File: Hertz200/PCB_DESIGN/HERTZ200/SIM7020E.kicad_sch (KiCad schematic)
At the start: 33 parts, among them J1 SMA_CONNECTOR, J2 SIM_Card, Q2 BC847, SW2 SW_Push, U2 SIM7020E, U3 TXB0104PW

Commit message: layout02
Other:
- moved on the sheet: D6
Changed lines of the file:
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@@
     (company "NANOHERTZ")
   )
-  (junction (at 41.91 127) (diameter 0) (color 0 0 0 0)
-  )
   (junction (at 78.74 163.83) (diameter 0) (color 0 0 0 0)
   )
@@
   (junction (at 199.39 113.03) (diameter 0) (color 0 0 0 0)
   )
+  (junction (at 86.36 124.46) (diameter 0) (color 0 0 0 0)
+  )
   (junction (at 41.91 110.49) (diameter 0) (color 0 0 0 0)
   )
-  (junction (at 31.75 110.49) (diameter 0) (color 0 0 0 0)
-  )
   (junction (at 52.07 124.46) (diameter 0) (color 0 0 0 0)
   )
@@
   )
   (junction (at 237.49 40.64) (diameter 0) (color 0 0 0 0)
+  )
+  (junction (at 97.79 110.49) (diameter 0) (color 0 0 0 0)
+  )
+  (junction (at 86.36 110.49) (diameter 0) (color 0 0 0 0)
   )
   (junction (at 74.93 124.46) (diameter 0) (color 0 0 0 0)
@@
     (stroke (width 0) (type default) (color 0 0 0 0))
   )
-  (wire (pts (xy 41.91 127) (xy 41.91 128.27))
+  (wire (pts (xy 41.91 124.46) (xy 41.91 128.27))
     (stroke (width 0) (type default) (color 0 0 0 0))
   )
@@
     (stroke (width 0) (type default) (color 0 0 0 0))
   )
+  (wire (pts (xy 86.36 127) (xy 86.36 124.46))
+    (stroke (width 0) (type default) (color 0 0 0 0))
+  )
+  (wire (pts (xy 97.79 127) (xy 86.36 127))
+    (stroke (width 0) (type default) (color 0 0 0 0))
+  )
   (wire (pts (xy 52.07 119.38) (xy 52.07 124.46))
     (stroke (width 0) (type default) (color 0 0 0 0))
@@
     (stroke (width 0) (type default) (color 0 0 0 0))
   )
-  (wire (pts (xy 31.75 127) (xy 41.91 127))
-    (stroke (width 0) (type default) (color 0 0 0 0))
-  )
   (wire (pts (xy 52.07 184.15) (xy 62.23 184.15))
     (stroke (width 0) (type default) (color 0 0 0 0))
   )
-  (wire (pts (xy 31.75 106.68) (xy 31.75 110.49))
-    (stroke (width 0) (type default) (color 0 0 0 0))
-  )
   (wire (pts (xy 139.7 162.56) (xy 140.97 162.56))
     (stroke (width 0) (type default) (color 0 0 0 0))
   )
+  (wire (pts (xy 86.36 110.49) (xy 97.79 110.49))
+    (stroke (width 0) (type default) (color 0 0 0 0))
+  )
   (wire (pts (xy 62.23 175.26) (xy 62.23 184.15))
     (stroke (width 0) (type default) (color 0 0 0 0))
@@
     (stroke (width 0) (type default) (color 0 0 0 0))
   )
-  (wire (pts (xy 31.75 111.76) (xy 31.75 110.49))
+  (wire (pts (xy 97.79 106.68) (xy 97.79 110.49))
     (stroke (width 0) (type default) (color 0 0 0 0))
   )
@@
   )
   (wire (pts (xy 229.87 100.33) (xy 226.06 100.33))
-    (stroke (width 0) (type default) (color 0 0 0 0))
-  )
-  (wire (pts (xy 31.75 110.49) (xy 41.91 110.49))
     (stroke (width 0) (type default) (color 0 0 0 0))
   )
@@
     (stroke (width 0) (type default) (color 0 0 0 0))
   )
-  (wire (pts (xy 41.91 124.46) (xy 41.91 127))
-    (stroke (width 0) (type default) (color 0 0 0 0))
-  )
   (wire (pts (xy 196.85 118.11) (xy 204.47 118.11))
     (stroke (width 0) (type default) (color 0 0 0 0))
@@
   )
   (wire (pts (xy 158.75 162.56) (xy 158.75 166.37))
+    (stroke (width 0) (type default) (color 0 0 0 0))
+  )
+  (wire (pts (xy 97.79 110.49) (xy 97.79 111.76))
     (stroke (width 0) (type default) (color 0 0 0 0))
   )
@@
     (effects (font (size 1.27 1.27)) (justify right bottom))
   )
-  (label "VBAT" (at 31.75 106.68 180)
+  (label "VBAT" (at 41.91 106.68 180)
     (effects (font (size 1.27 1.27)) (justify right bottom))
   )
@@
     (pin "2")
   )
-  (symbol (lib_id "ESD:ESD3V3D9-TP") (at 31.75 111.76 270) (unit 1)
-    (in_bom yes) (on_board yes)
-    (property "Reference" "D6" (id 0) (at 25.4 121.92 90)
-      (effects (font (size 1.27 1.27)) (justify left))
-    )
-    (property "Value" "ESD" (id 1) (at 25.4 124.46 90)
-      (effects (font (size 1.27 1.27)) (justify left))
-    )
-    (property "Footprint" "Diode_SMD:D_0603_1608Metric" (id 2) (at 35.56 121.92 0)
-      (effects (font (size 1.27 1.27)) (justify left) hide)
-    )
-    (property "Datasheet" "https://www.mouser.jp/datasheet/2/258/ESD3V3D9(SOD-923)-479119.pdf" (id 3) (at 33.02 121.92 0)
-      (effects (font (size 1.27 1.27)) (justify left) hide)
-    )
-    (property "Description" "ESD Suppressors / TVS Diodes Uni-dir 10mA, 3.3V" (id 4) (at 30.48 121.92 0)
-      (effects (font (size 1.27 1.27)) (justify left) hide)
-    )
-    (property "Height" "0.43" (id 5) (at 27.94 121.92 0)
-      (effects (font (size 1.27 1.27)) (justify left) hide)
-    )
-    (property "Manufacturer_Name" "Micro Commercial Components (MCC)" (id 6) (at 25.4 121.92 0)
-      (effects (font (size 1.27 1.27)) (justify left) hide)
-    )
-    (property "Manufacturer_Part_Number" "ESD3V3D9-TP" (id 7) (at 22.86 121.92 0)
-      (effects (font (size 1.27 1.27)) (justify left) hide)
-    )
-    (property "Mouser Part Number" "833-ESD3V3D9-TP" (id 8) (at 20.32 121.92 0)
-      (effects (font (size 1.27 1.27)) (justify left) hide)
-    )
-    (property "Mouser Price/Stock" "https://www.mouser.co.uk/ProductDetail/Micro-Commercial-Components-MCC/ESD3V3D9-TP?qs=WJd%252B7yD6my3RbvY7hgxwaQ%3D%3D" (id 9) (at 17.78 121.92 0)
-      (effects (font (size 1.27 1.27)) (justify left) hide)
-    )
-    (property "Arrow Part Number" "ESD3V3D9-TP" (id 10) (at 15.24 121.92 0)
-      (effects (font (size 1.27 1.27)) (justify left) hide)
-    )
-    (property "Arrow Price/Stock" "https://www.arrow.com/en/products/esd3v3d9-tp/micro-commercial-components" (id 11) (at 12.7 121.92 0)
+  (symbol (lib_id "ESD:ESD3V3D9-TP") (at 97.79 111.76 270) (unit 1)
+    (in_bom yes) (on_board yes)
+    (property "Reference" "D6" (id 0) (at 101.6 115.57 90)
+      (effects (font (size 1.27 1.27)) (justify left))
+    )
+    (property "Value" "ESD" (id 1) (at 101.6 119.38 90)
+      (effects (font (size 1.27 1.27)) (justify left))
+    )
+    (property "Footprint" "Diode_SMD:D_0603_1608Metric" (id 2) (at 101.6 121.92 0)
+      (effects (font (size 1.27 1.27)) (justify left) hide)
+    )
+    (property "Datasheet" "https://www.mouser.jp/datasheet/2/258/ESD3V3D9(SOD-923)-479119.pdf" (id 3) (at 99.06 121.92 0)
+      (effects (font (size 1.27 1.27)) (justify left) hide)
+    )
+    (property "Description" "ESD Suppressors / TVS Diodes Uni-dir 10mA, 3.3V" (id 4) (at 96.52 121.92 0)
+      (effects (font (size 1.27 1.27)) (justify left) hide)
+    )
+    (property "Height" "0.43" (id 5) (at 93.98 121.92 0)
+      (effects (font (size 1.27 1.27)) (justify left) hide)
+    )
+    (property "Manufacturer_Name" "Micro Commercial Components (MCC)" (id 6) (at 91.44 121.92 0)
+      (effects (font (size 1.27 1.27)) (justify left) hide)
+    )
+    (property "Manufacturer_Part_Number" "ESD3V3D9-TP" (id 7) (at 88.9 121.92 0)
+      (effects (font (size 1.27 1.27)) (justify left) hide)
+    )
+    (property "Mouser Part Number" "833-ESD3V3D9-TP" (id 8) (at 86.36 121.92 0)
+      (effects (font (size 1.27 1.27)) (justify left) hide)
+    )
+    (property "Mouser Price/Stock" "https://www.mouser.co.uk/ProductDetail/Micro-Commercial-Components-MCC/ESD3V3D9-TP?qs=WJd%252B7yD6my3RbvY7hgxwaQ%3D%3D" (id 9) (at 83.82 121.92 0)
+      (effects (font (size 1.27 1.27)) (justify left) hide)
+    )
+    (property "Arrow Part Number" "ESD3V3D9-TP" (id 10) (at 81.28 121.92 0)
+      (effects (font (size 1.27 1.27)) (justify left) hide)
+    )
+    (property "Arrow Price/Stock" "https://www.arrow.com/en/products/esd3v3d9-tp/micro-commercial-components" (id 11) (at 78.74 121.92 0)
       (effects (font (size 1.27 1.27)) (justify left) hide)
     )
@@
     (pin "9")
   )
-  (symbol (lib_id "power:+3.3V") (at 41.91 106.68 0) (unit 1)
-    (in_bom yes) (on_board yes) (fields_autoplaced)
-    (property "Reference" "#PWR09" (id 0) (at 41.91 110.49 0)
-      (effects (font (size 1.27 1.27)) hide)
-    )
-    (property "Value" "+3.3V" (id 1) (at 41.91 101.6 0))
-    (property "Footprint" "" (id 2) (at 41.91 106.68 0)
-      (effects (font (size 1.27 1.27)) hide)
-    )
-    (property "Datasheet" "" (id 3) (at 41.91 106.68 0)
-      (effects (font (size 1.27 1.27)) hide)
-    )
+  (symbol (lib_id "power:+3.3V") (at 97.79 106.68 0) (unit 1)
+    (in_bom yes) (on_board yes) (fields_autoplaced)
+    (property "Reference" "#PWR09" (id 0) (at 97.79 110.49 0)
+      (effects (font (size 1.27 1.27)) hide)
+    )
+    (property "Value" "+3.3V" (id 1) (at 97.79 101.6 0))
+    (property "Footprint" "" (id 2) (at 97.79 106.68 0)
+      (effects (font (size 1.27 1.27)) hide)
+    )
+    (property "Datasheet" "" (id 3) (at 97.79 106.68 0)
+      (effects (font (size 1.27 1.27)) hide)
+    )

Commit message: DRC
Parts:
- removed SW2: SW_Push, TS04-66-75-BK-160-SMT:SW_TS04-66-75-BK-160-SMT, symbol Switch:SW_Push
- added D7, D9: ESD9L5.0ST5G, ESD9L5:DIOM1006X40N, symbol ESD9L5.0ST5G:ESD9L5.0ST5G
- added J5: 105164-0001, 105164-0001:MOLEX_105164-0001, symbol 105164-0001:105164-0001
- added R24: 33K, Resistor_SMD:R_0603_1608Metric, symbol Device:R_Small
- added S2: TL3305AF160QG, TL3305AF160QG:SW_TL3305AF160QG, symbol TL3305AF160QG:TL3305AF160QG
- D3: value ESD -> LXES15AAA1-153; footprint Diode_SMD:D_0603_1608Metric -> Diode_SMD:D_0402_1005Metric
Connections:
- net GND: now also D7.A, D9.A, J5.5, R24.1, S2.1, S2.2
- net PWRKEY: now also S2.3, S2.4
- net SIM7020E_D+: now reaches U2.25 (USB_DP)
- net SIM7020E_D+: now also D7.C, J5.3
- net SIM7020E_D-: now reaches U2.26 (USB_DM)
- net SIM7020E_D-: now also D9.C, J5.2
- new net: J5.SH1 (SHIELD), J5.SH2 (SHIELD), J5.SH3 (SHIELD), J5.SH4 (SHIELD), J5.SH5 (SHIELD), J5.SH6 (SHIELD), R24.2

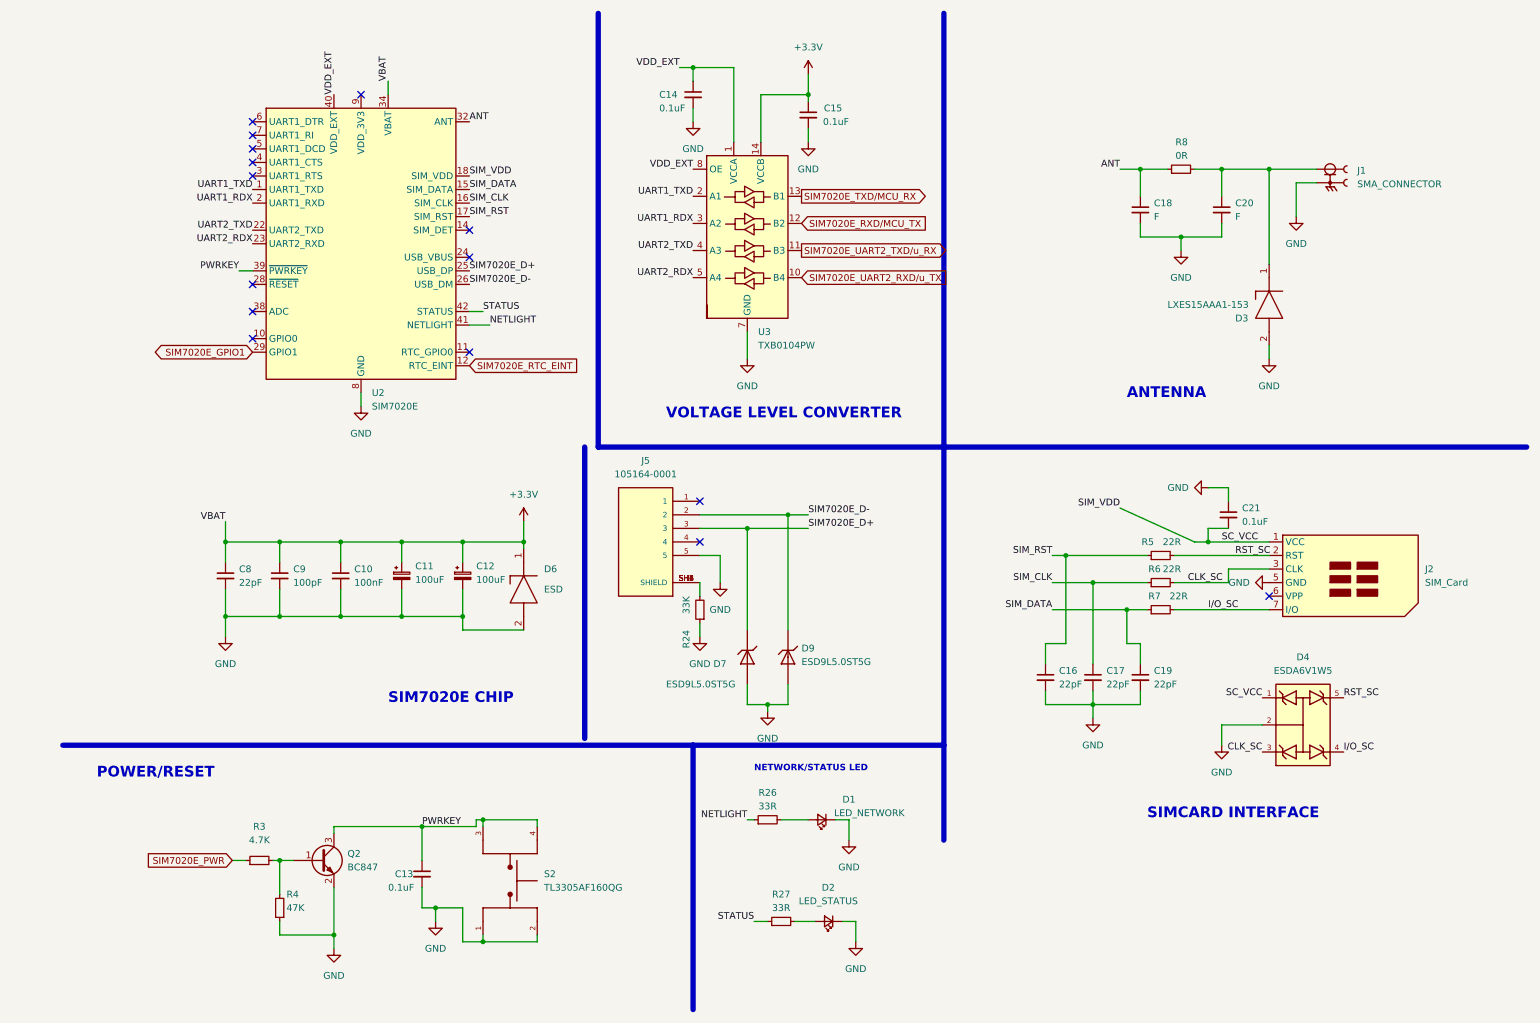
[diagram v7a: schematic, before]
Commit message: TEMPERATURE SENSOR ROUTING
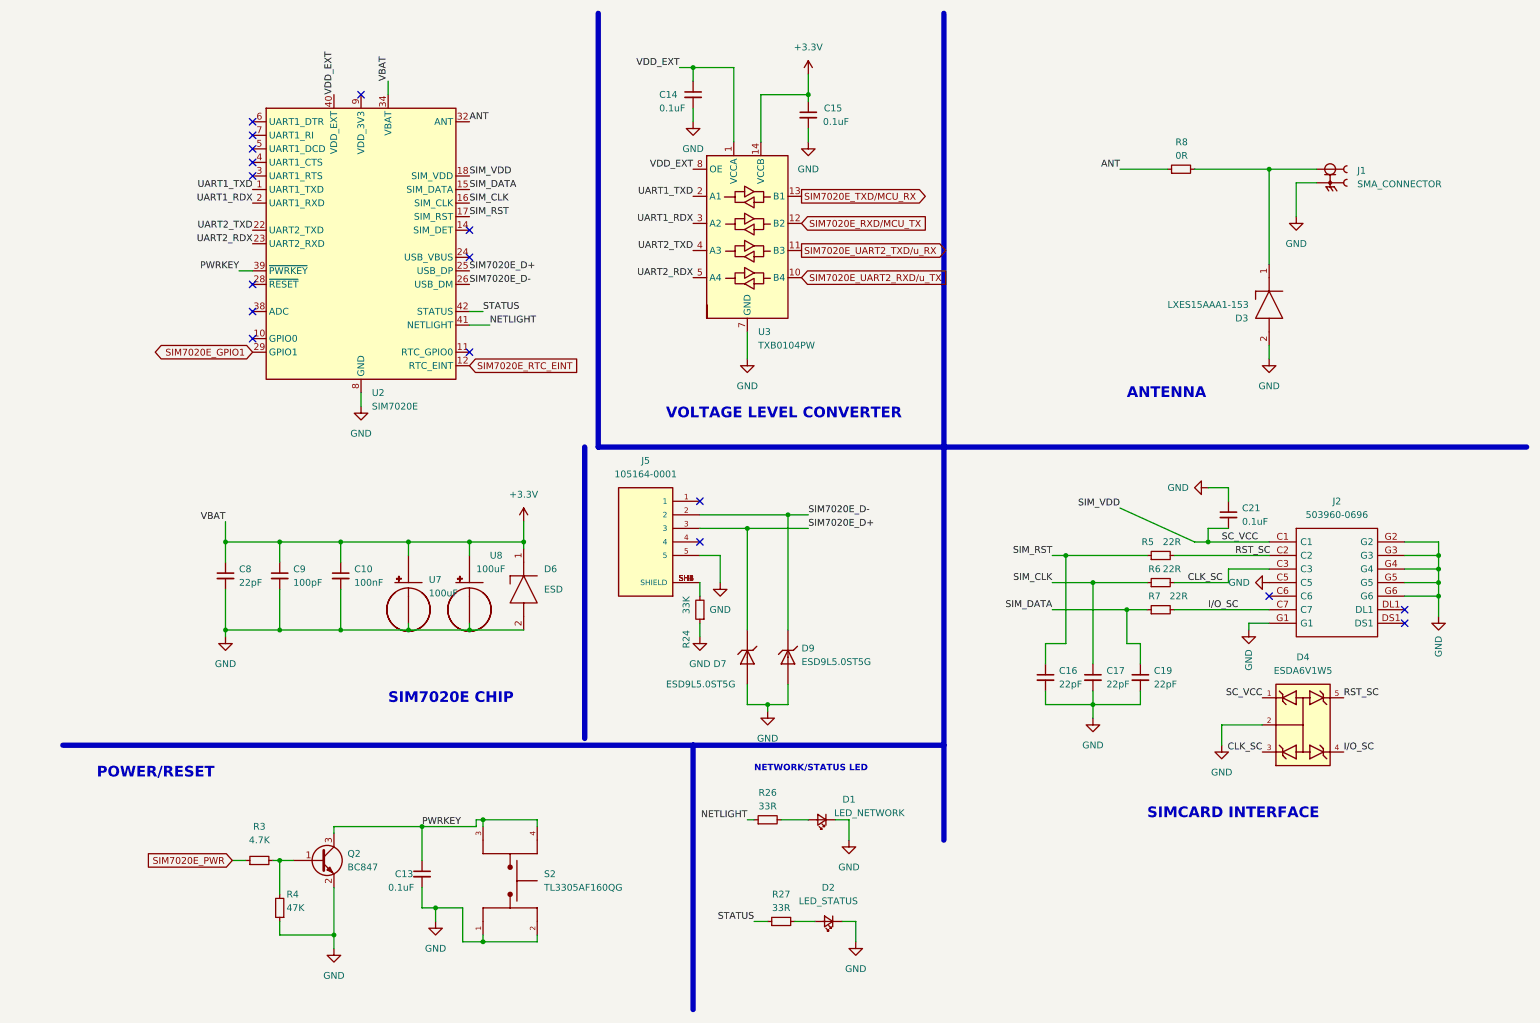
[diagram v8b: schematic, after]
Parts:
- removed C11, C12: 100uF, T491X107K025AT:CAPMP7343X400N, symbol Device:C_Polarized_Small
- removed C18, C20: F, Capacitor_SMD:C_0603_1608Metric, symbol Device:C_Small
- removed J2: SIM_Card, 503960-0696:5039600696, symbol Connector:SIM_Card
- added J2: 503960-0696, 503960-0696:5039600696, symbol 503960-0696:503960-0696
- added U7, U8: 100uF, T491X107K025AT:CAPMP7343X400N, symbol T491X107K025AT:T491X107K025AT
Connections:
- net +3V3: now also U7.+, U8.+
- net CLK_SC: now also J2.C3
- net GND: now also J2.C5, J2.G1, J2.G2, J2.G3, J2.G4, J2.G5, J2.G6, U7.-, U8.-
- net I/O_SC: now also J2.C7
- net RST_SC: now also J2.C2
- net SC_VCC: now also J2.C1
- no-connect marks 15 -> 17
